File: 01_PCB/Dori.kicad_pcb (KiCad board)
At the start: 2 copper layers, 306.4 x 111.1 mm, 206 parts, among them J1 TYPE-C-31-M12_13, J2 AVR-ISP-6_mod, J3 4PIN, J4 4PIN, J5 TYPE-C-31-M12_13, J6 AVR-ISP-6_mod, K1 KEYSW, K10 KEYSW, K11 KEYSW, K12 KEYSW, K13 KEYSW, K14 KEYSW, K15 KEYSW, K16 KEYSW, K17 KEYSW, K18 KEYSW, K19 KEYSW, K2 KEYSW, K20 KEYSW, K21 KEYSW, K22 KEYSW, K23 KEYSW, K24 KEYSW, K25 KEYSW, K26 KEYSW, K27 KEYSW, K28 KEYSW, K29 KEYSW, K3 KEYSW, K30 KEYSW, K31 KEYSW, K32 KEYSW, K33 KEYSW, K34 KEYSW, K35 KEYSW, K36 KEYSW, K37 KEYSW, K38 KEYSW, K39 KEYSW, K4 KEYSW, K40 KEYSW, K41 KEYSW, K42 KEYSW, K43 KEYSW, K44 KEYSW, K45 KEYSW, K46 KEYSW, K47 KEYSW, K48 KEYSW, K49 KEYSW, K5 KEYSW, K50 KEYSW, K51 KEYSW, K52 KEYSW, K53 KEYSW, K54 KEYSW, K55 KEYSW, K56 KEYSW, K6 KEYSW, K7 KEYSW, K8 KEYSW, K9 KEYSW, SW1 SW_PUSH, SW10 Rotary_Encoder_Switch, SW2 SW_PUSH, SW3 Rotary_Encoder_Switch, SW4 Rotary_Encoder_Switch, SW5 Rotary_Encoder_Switch, SW6 Rotary_Encoder_Switch, SW7 Rotary_Encoder_Switch, SW8 Rotary_Encoder_Switch, SW9 Rotary_Encoder_Switch, U1 ATMEGA32U4, U10 HOLE, U11 HOLE, U12 ATMEGA32U4, U13 HOLE, U14 HOLE, U15 HOLE, U16 HOLE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

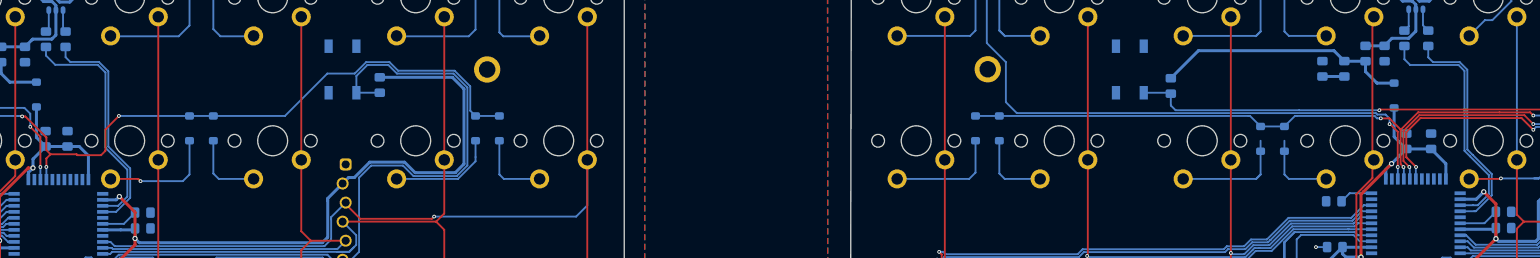
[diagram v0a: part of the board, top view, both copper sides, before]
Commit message: Routed data lines as differential pair
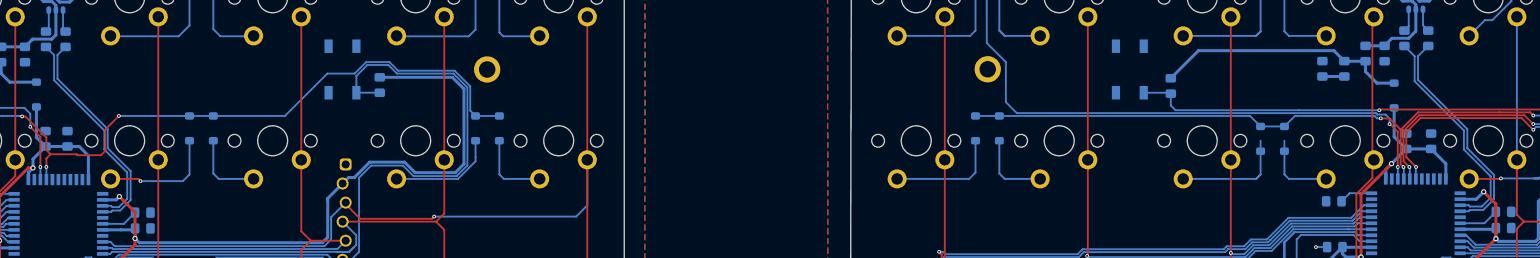
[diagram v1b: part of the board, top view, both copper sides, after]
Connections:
- net D+BUSa renamed DBUSa+
- net D+BUSb renamed DBUSb+
- net D+a renamed Net-(R3-Pad2)
- net D+b renamed Net-(R11-Pad2)
- net D-BUSa renamed DBUSa-
- net D-BUSb renamed DBUSb-
- net D-a renamed Net-(R2-Pad2)
- net D-b renamed Net-(R10-Pad2)
- net Net-(R10-Pad1) renamed Db-
- net Net-(R11-Pad1) renamed Db+
- net Net-(R2-Pad1) renamed Da-
- net Net-(R3-Pad1) renamed Da+
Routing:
- net Da-: track 31.5 -> 28.5 mm
- net Db-: track 32.6 -> 29.6 mm
- net Da+: track 30.3 -> 29.3 mm
